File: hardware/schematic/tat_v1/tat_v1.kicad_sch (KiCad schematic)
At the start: 12 parts, among them SW1 SW_SPDT, SW2 SW_Push, U1 STM32U073CCUx

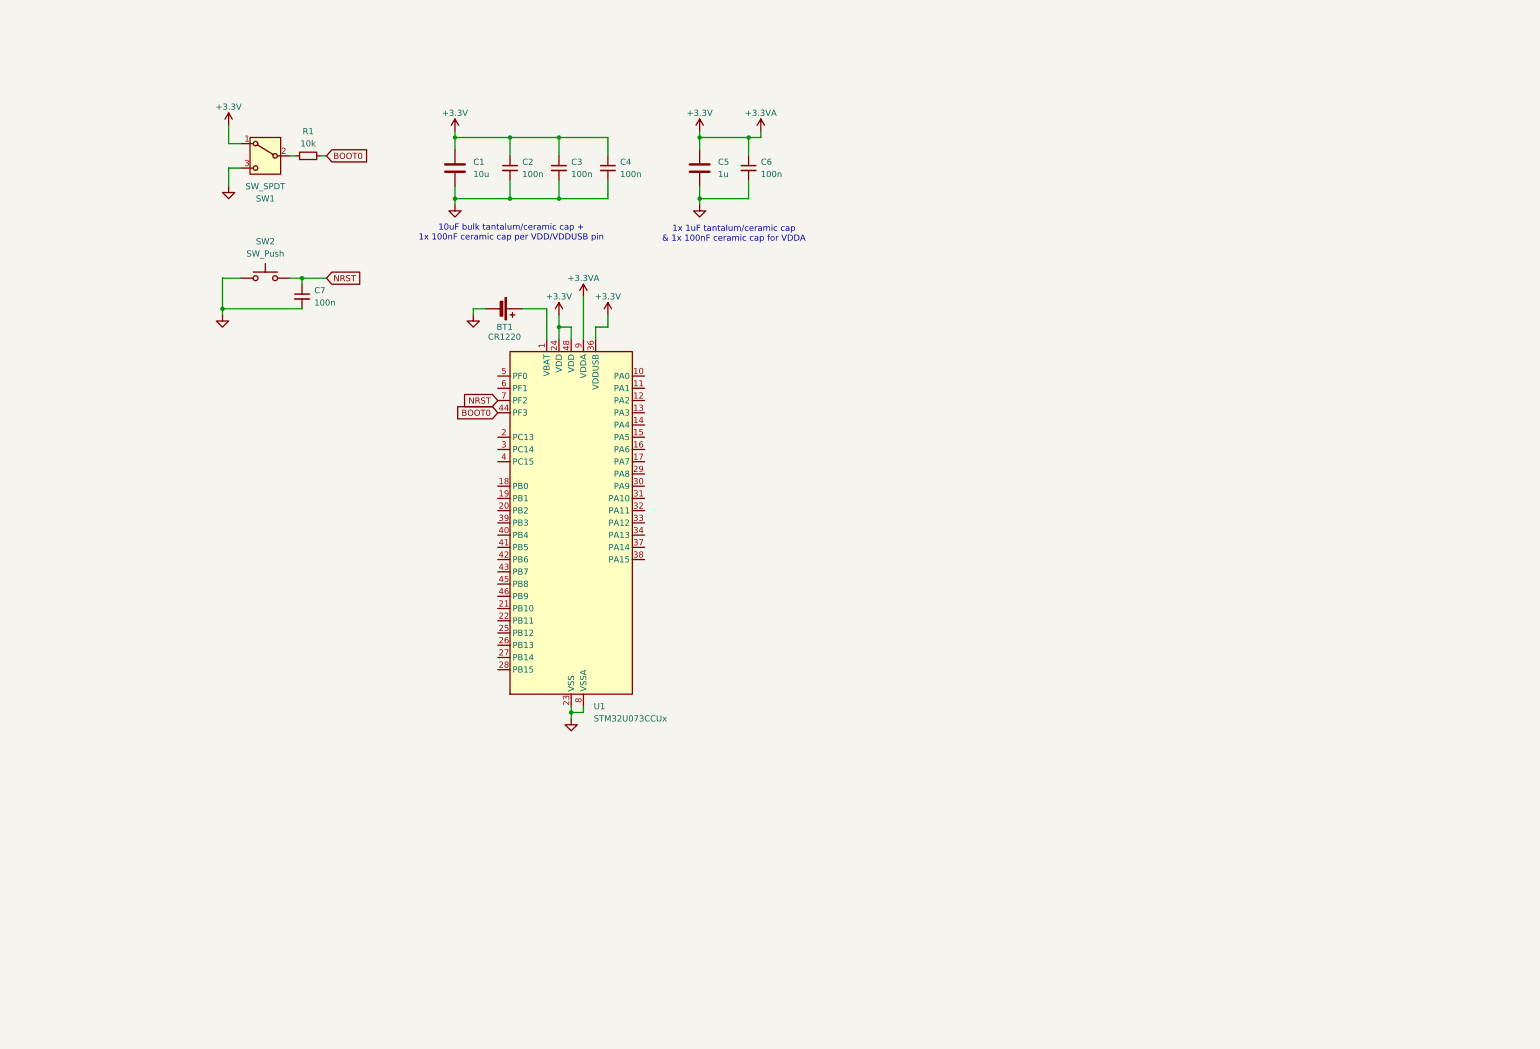
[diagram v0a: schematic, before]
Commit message: Working on KiCAD schematic
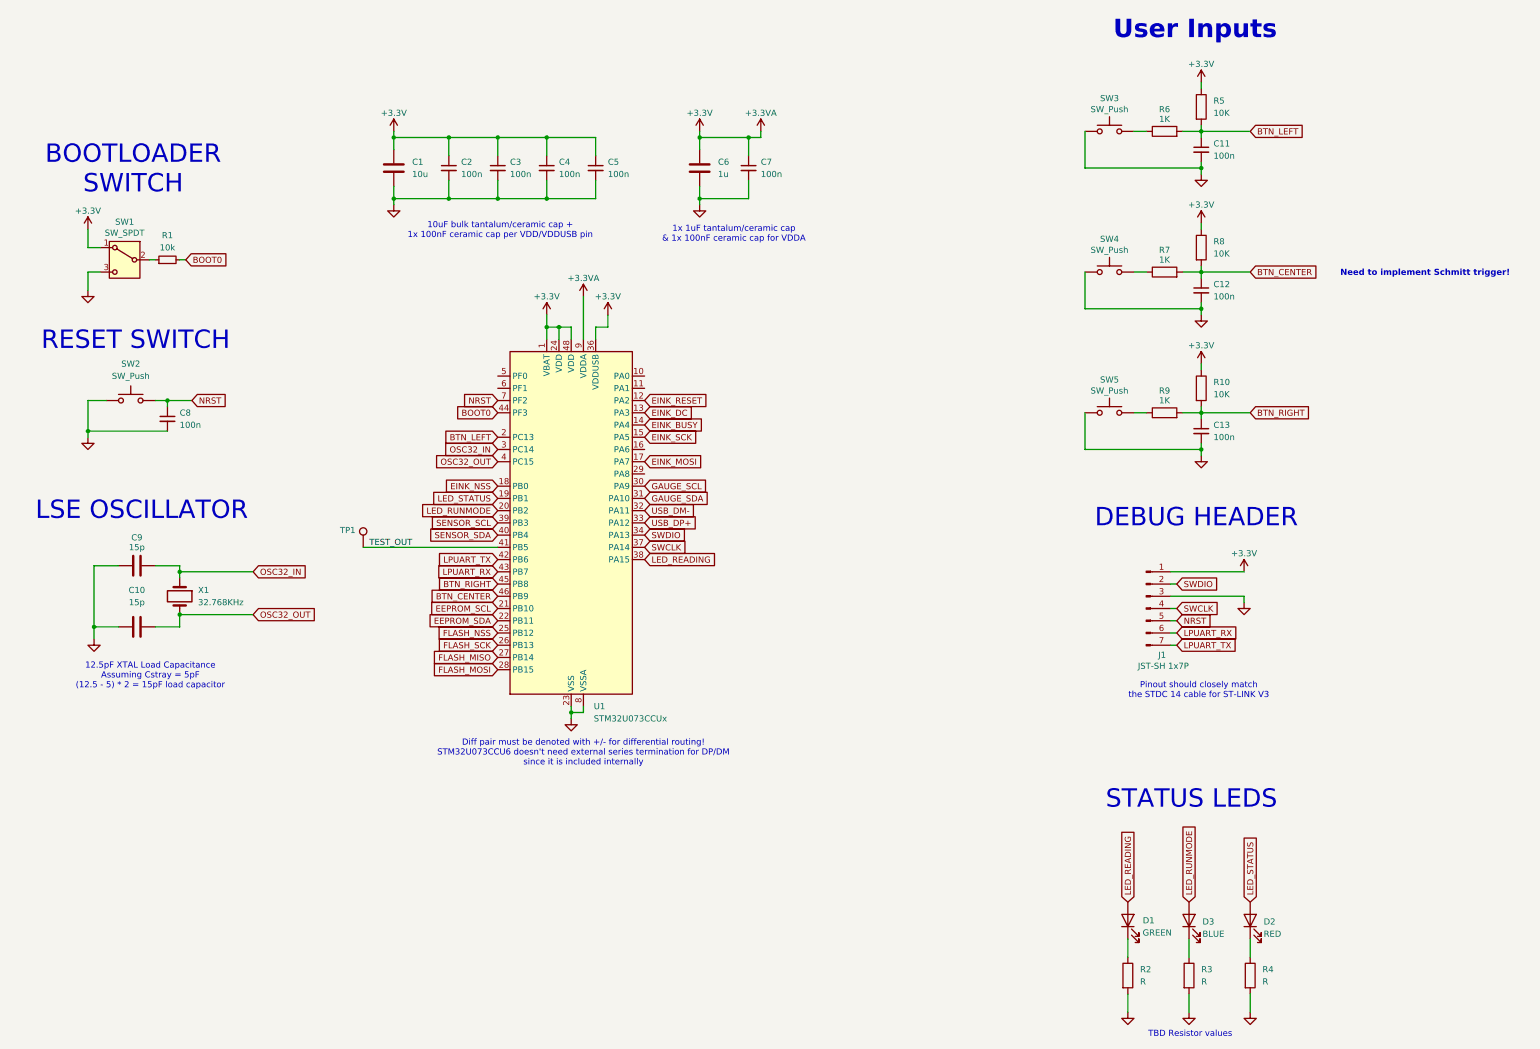
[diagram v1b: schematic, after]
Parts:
- removed BT1: CR1220, symbol Device:Battery_Cell
- added C10, C9: 15p, symbol Device:C
- added C11, C12, C13, C5: 100n, symbol Device:C_Small
- added D1: GREEN, symbol Device:LED
- added D2: RED, symbol Device:LED
- added D3: BLUE, symbol Device:LED
- added J1: JST-SH 1x7P, symbol Connector:Conn_01x07_Pin
- added R10, R5, R8: 10K, symbol Device:R
- added R2, R3, R4: R, symbol Device:R
- added R6, R7, R9: 1K, symbol Device:R
- added SW3, SW4, SW5: SW_Push, symbol Switch:SW_Push
- added TP1: TestPoint, symbol Connector:TestPoint
- added X1: 32.768KHz, symbol Device:Crystal
- renumbered C5 to C6, C6 to C7, C7 to C8
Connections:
- net +3.3V: now also U1.1 (VBAT), C5.1, J1.1 (Pin_1), R10.1, R5.1, R8.1
- net GND: now also C10.1, C11.2, C12.2, C13.2, C5.2, C9.1, J1.3 (Pin_3), R2.2, R3.2, R4.2, SW3.1, SW4.1, SW5.1
- net NRST: now also J1.5 (Pin_5)
- net EINK_RESET: now reaches U1.12 (PA2)
- net EINK_DC: now reaches U1.13 (PA3)
- net EINK_BUSY: now reaches U1.14 (PA4)
- net EINK_SCK: now reaches U1.15 (PA5)
- net EINK_MOSI: now reaches U1.17 (PA7)
- net EINK_NSS: now reaches U1.18 (PB0)
- net LED_STATUS: now reaches U1.19 (PB1)
- net LED_STATUS: now also D2.2 (A)
- net BTN_LEFT: now reaches U1.2 (PC13)
- net BTN_LEFT: now also C11.1, R5.2, R6.2
- net LED_RUNMODE: now reaches U1.20 (PB2)
- net LED_RUNMODE: now also D3.2 (A)
- net EEPROM_SCL: now reaches U1.21 (PB10)
- net EEPROM_SDA: now reaches U1.22 (PB11)
- net FLASH_NSS: now reaches U1.25 (PB12)
- net FLASH_SCK: now reaches U1.26 (PB13)
- net FLASH_MISO: now reaches U1.27 (PB14)
- net FLASH_MOSI: now reaches U1.28 (PB15)
- net OSC32_IN: now reaches U1.3 (PC14)
- net OSC32_IN: now also C9.2, X1.1
- net GAUGE_SCL: now reaches U1.30 (PA9)
- net GAUGE_SDA: now reaches U1.31 (PA10)
- net USB_DM-: now reaches U1.32 (PA11)
- net USB_DP+: now reaches U1.33 (PA12)
- net SWDIO: now reaches U1.34 (PA13)
- net SWDIO: now also J1.2 (Pin_2)
- net SWCLK: now reaches U1.37 (PA14)
- net SWCLK: now also J1.4 (Pin_4)
- net LED_READING: now reaches U1.38 (PA15)
- net LED_READING: now also D1.2 (A)
- net SENSOR_SCL: now reaches U1.39 (PB3)
- net OSC32_OUT: now reaches U1.4 (PC15)
- net OSC32_OUT: now also C10.2, X1.2
- net SENSOR_SDA: now reaches U1.40 (PB4)
- net TEST_OUT: now reaches U1.41 (PB5)
- net TEST_OUT: now also TP1.1
- net LPUART_TX: now reaches U1.42 (PB6)
- net LPUART_TX: now also J1.7 (Pin_7)
- net LPUART_RX: now reaches U1.43 (PB7)
- net LPUART_RX: now also J1.6 (Pin_6)
- net BTN_RIGHT: now reaches U1.45 (PB8)
- net BTN_RIGHT: now also C13.1, R10.2, R9.2
- net BTN_CENTER: now reaches U1.46 (PB9)
- net BTN_CENTER: now also C12.1, R7.2, R8.2
- new net: R9.1, SW5.2
- new net: D1.1 (K), R2.1
- new net: R7.1, SW4.2
- new net: R6.1, SW3.2
- new net: D2.1 (K), R4.1
- new net: D3.1 (K), R3.1
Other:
- note added: "12.5pF XTAL Load Capacitance Assuming Cstray = 5pF (12.5 - 5) * 2 = 15pF load capacitor"
- note added: "BOOTLOADER SWITCH"
- note added: "DEBUG HEADER"
- note added: "Diff pair must be denoted with +/- for differential routing! STM32U073CCU6 doesn't need external series termination for DP/DM since it is included internally"
- note added: "LSE OSCILLATOR"
- note added: "Need to implement Schmitt trigger!"
- note added: "Pinout should closely match the STDC 14 cable for ST-LINK V3"
- note added: "RESET SWITCH"
- note added: "STATUS LEDS"
- note added: "TBD Resistor values"
- note added: "User Inputs"
- moved on the sheet: C1, C2, C3, C4, C8, R1, SW1, SW2

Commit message: Added NPM1300, needs completion
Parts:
- removed C1: 10u, symbol Device:C
- removed C10, C9: 15p, symbol Device:C
- removed C11, C12, C13, C2, C3, C4, C5, C7, C8: 100n, symbol Device:C_Small
- removed C6: 1u, symbol Device:C
- removed D1: GREEN, symbol Device:LED
- removed D2: RED, symbol Device:LED
- removed D3: BLUE, symbol Device:LED
- removed J1: JST-SH 1x7P, symbol Connector:Conn_01x07_Pin
- removed R1: 10k, symbol Device:R_Small
- removed R10, R5, R8: 10K, symbol Device:R
- removed R2, R3, R4: R, symbol Device:R
- removed R6, R7, R9: 1K, symbol Device:R
- removed SW1: SW_SPDT, symbol Switch:SW_SPDT
- removed SW2, SW3, SW4, SW5: SW_Push, symbol Switch:SW_Push
- removed TP1: TestPoint, symbol Connector:TestPoint
- removed U1: STM32U073CCUx, Package_DFN_QFN:QFN-48-1EP_7x7mm_P0.5mm_EP5.6x5.6mm, symbol MCU_ST_STM32U0:STM32U073CCUx
- removed X1: 32.768KHz, symbol Device:Crystal
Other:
- added sheet MCU (MCU.kicad_sch)
- added sheet Peripherals and user input (peripherals.kicad_sch)
- added sheet Power (untitled.kicad_sch)
- note removed: "10uF bulk tantalum/ceramic cap + 1x 100nF ceramic cap per VDD/VDDUSB pin"
- note removed: "12.5pF XTAL Load Capacitance Assuming Cstray = 5pF (12.5 - 5) * 2 = 15pF load capacitor"
- note removed: "1x 1uF tantalum/ceramic cap & 1x 100nF ceramic cap for VDDA"
- note removed: "BOOTLOADER SWITCH"
- note removed: "DEBUG HEADER"
- note removed: "Diff pair must be denoted with +/- for differential routing! STM32U073CCU6 doesn't need external series termination for DP/DM since it is included internally"
- note removed: "LSE OSCILLATOR"
- note removed: "Need to implement Schmitt trigger!"
- note removed: "Pinout should closely match the STDC 14 cable for ST-LINK V3"
- note removed: "RESET SWITCH"
- note removed: "STATUS LEDS"
- note removed: "TBD Resistor values"
- note removed: "User Inputs"

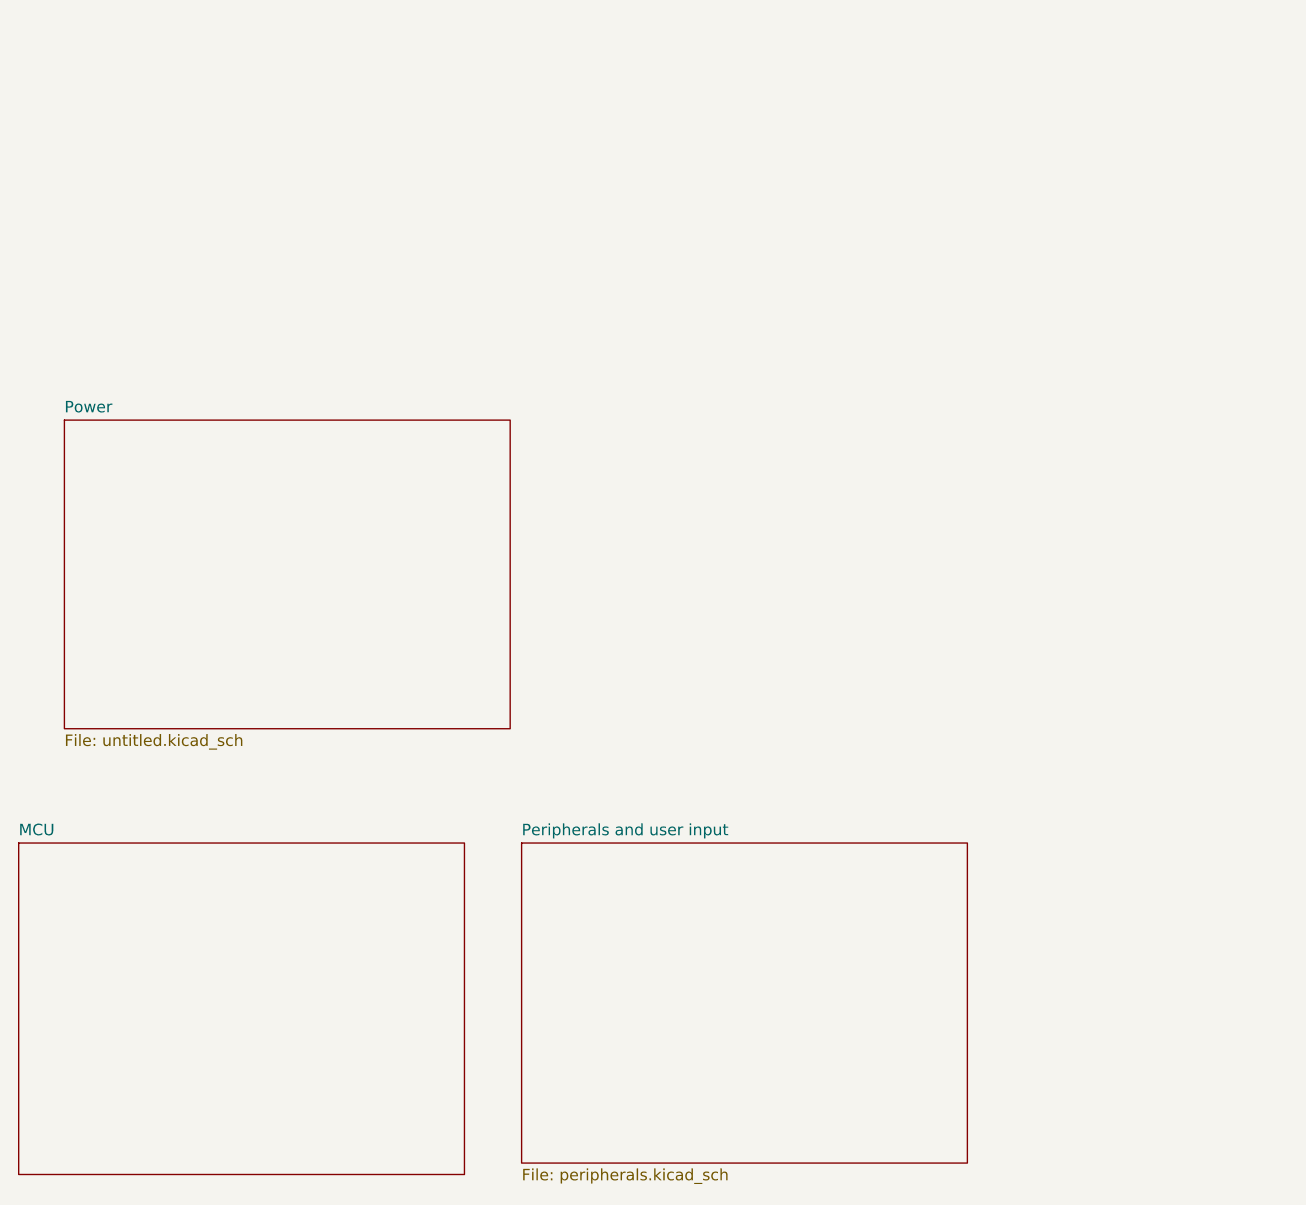
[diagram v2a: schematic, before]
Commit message: Simplified partslist and working on updated schematic
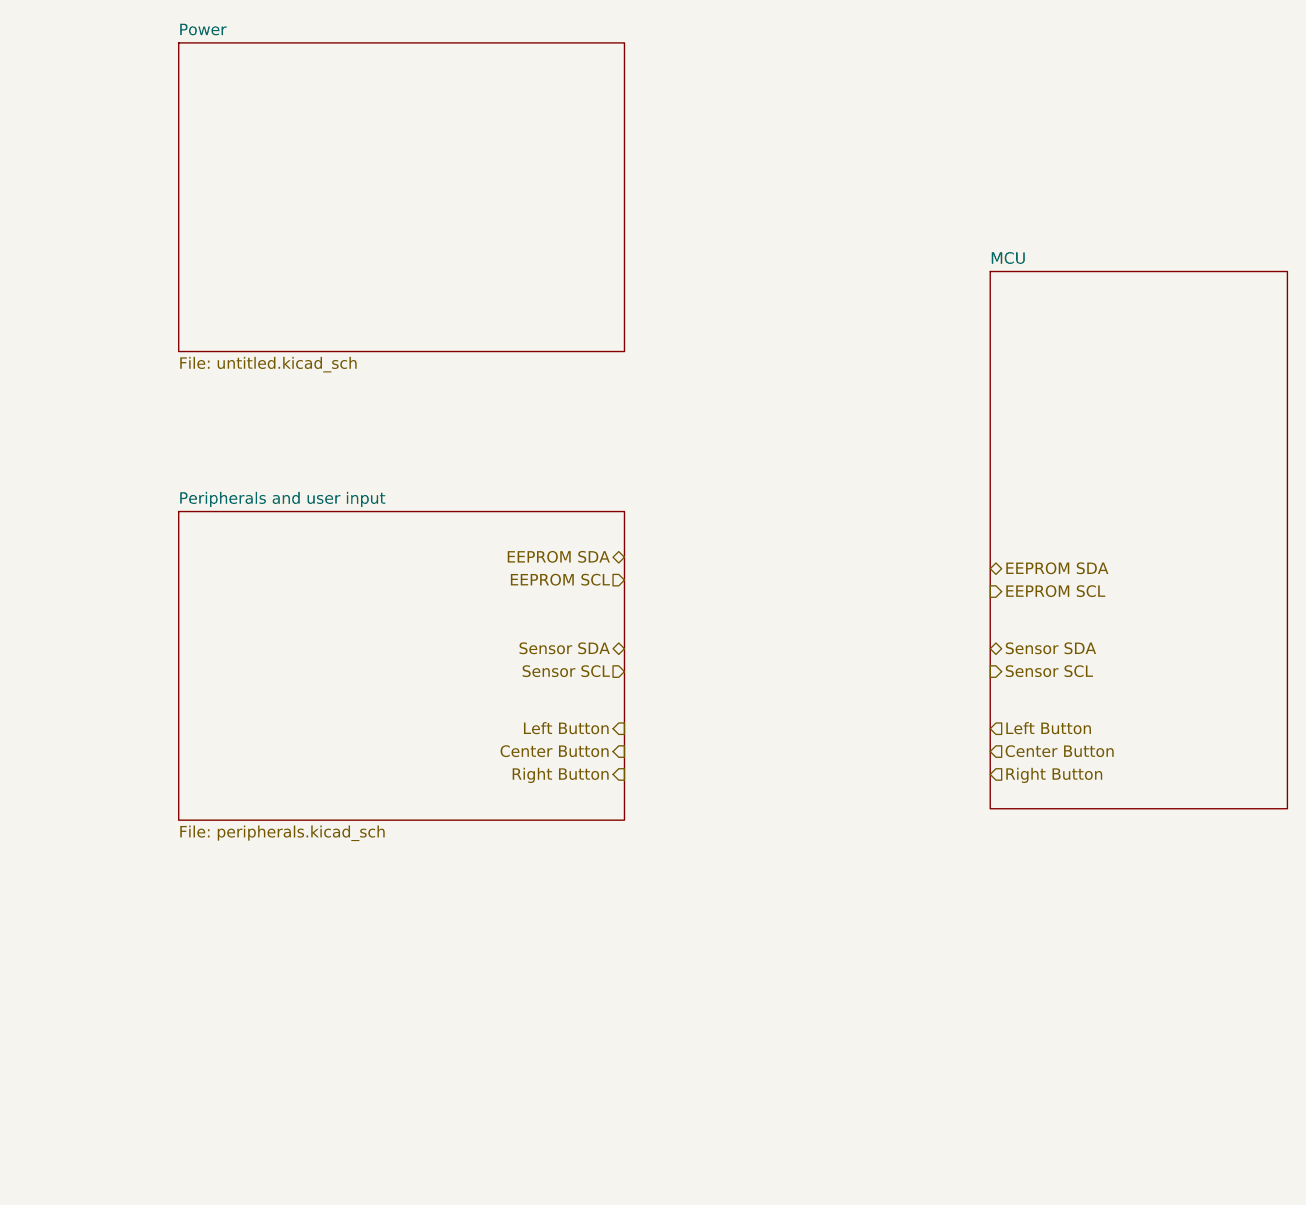
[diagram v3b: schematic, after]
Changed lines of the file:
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@@
 		(rev "v1.0")
 	)
+	(hierarchical_label "Sensor SCL"
+		(shape output)
+		(at 123.19 139.7 0)
+		(effects
+			(font
+				(size 1.27 1.27)
+			)
+			(justify left)
+		)
+	)
+	(hierarchical_label "EEPROM SCL"
+		(shape input)
+		(at 82.55 129.54 180)
+		(effects
+			(font
+				(size 1.27 1.27)
+			)
+			(justify right)
+		)
+	)
+	(hierarchical_label "Left Button"
+		(shape output)
+		(at 82.55 146.05 180)
+		(effects
+			(font
+				(size 1.27 1.27)
+			)
+			(justify right)
+		)
+	)
+	(hierarchical_label "Center Button"
+		(shape input)
+		(at 123.19 148.59 0)
+		(effects
+			(font
+				(size 1.27 1.27)
+			)
+			(justify left)
+		)
+	)
+	(hierarchical_label "Sensor SCL"
+		(shape input)
+		(at 82.55 139.7 180)
+		(effects
+			(font
+				(size 1.27 1.27)
+			)
+			(justify right)
+		)
+	)
+	(hierarchical_label "EEPROM SCL"
+		(shape output)
+		(at 123.19 130.81 0)
+		(effects
+			(font
+				(size 1.27 1.27)
+			)
+			(justify left)
+		)
+	)
+	(hierarchical_label "EEPROM SDA"
+		(shape bidirectional)
+		(at 123.19 128.27 0)
+		(effects
+			(font
+				(size 1.27 1.27)
+			)
+			(justify left)
+		)
+	)
+	(hierarchical_label "Right Button"
+		(shape input)
+		(at 123.19 151.13 0)
+		(effects
+			(font
+				(size 1.27 1.27)
+			)
+			(justify left)
+		)
+	)
+	(hierarchical_label "Sensor SDA"
+		(shape bidirectional)
+		(at 123.19 137.16 0)
+		(effects
+			(font
+				(size 1.27 1.27)
+			)
+			(justify left)
+		)
+	)
+	(hierarchical_label "EEPROM SDA"
+		(shape bidirectional)
+		(at 82.55 127 180)
+		(effects
+			(font
+				(size 1.27 1.27)
+			)
+			(justify right)
+		)
+	)
+	(hierarchical_label "Left Button"
+		(shape input)
+		(at 123.19 146.05 0)
+		(effects
+			(font
+				(size 1.27 1.27)
+			)
+			(justify left)
+		)
+	)
+	(hierarchical_label "Right Button"
+		(shape output)
+		(at 82.55 151.13 180)
+		(effects
+			(font
+				(size 1.27 1.27)
+			)
+			(justify right)
+		)
+	)
+	(hierarchical_label "Sensor SDA"
+		(shape bidirectional)
+		(at 82.55 137.16 180)
+		(effects
+			(font
+				(size 1.27 1.27)
+			)
+			(justify right)
+		)
+	)
+	(hierarchical_label "Center Button"
+		(shape output)
+		(at 82.55 148.59 180)
+		(effects
+			(font
+				(size 1.27 1.27)
+			)
+			(justify right)
+		)
+	)
 	(sheet
-		(at 20.32 111.76)
+		(at 33.02 69.85)
 		(size 49.53 34.29)
 		(exclude_from_sim no)
@@
 		)
 		(property "Sheetname" "Power"
-			(at 20.32 111.0484 0)
+			(at 33.02 69.1384 0)
 			(effects
 				(font
@@
 		)
 		(property "Sheetfile" "untitled.kicad_sch"
-			(at 20.32 146.6346 0)
+			(at 33.02 104.7246 0)
 			(effects
 				(font
@@
 	)
 	(sheet
-		(at 15.24 158.75)
-		(size 49.53 36.83)
+		(at 123.19 95.25)
+		(size 33.02 59.69)
 		(exclude_from_sim no)
 		(in_bom yes)
@@
 		)
 		(property "Sheetname" "MCU"
-			(at 15.24 158.0384 0)
+			(at 123.19 94.5384 0)
 			(effects
 				(font
@@
 		)
 		(property "Sheetfile" "MCU.kicad_sch"
-			(at 15.24 196.1646 0)
+			(at 123.19 155.5246 0)
 			(effects
 				(font
@@
 	)
 	(sheet
-		(at 71.12 158.75)
-		(size 49.53 35.56)
+		(at 33.02 121.92)
+		(size 49.53 34.29)
 		(exclude_from_sim no)
 		(in_bom yes)
@@
 		)
 		(property "Sheetname" "Peripherals and user input"
-			(at 71.12 158.0384 0)
+			(at 33.02 121.2084 0)
 			(effects
 				(font
@@
 		)
 		(property "Sheetfile" "peripherals.kicad_sch"
-			(at 71.12 194.8946 0)
-			(effects
-				(font
+			(at 33.02 156.7946 0)
+			(effects
+				(font

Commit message: Basic circuit is complete, needs double checking
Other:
- added sheet Display (display.kicad_sch)
